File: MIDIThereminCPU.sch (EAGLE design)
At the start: 5 parts, among them Q1 16MHz, U1 ATMEGA328P-AU

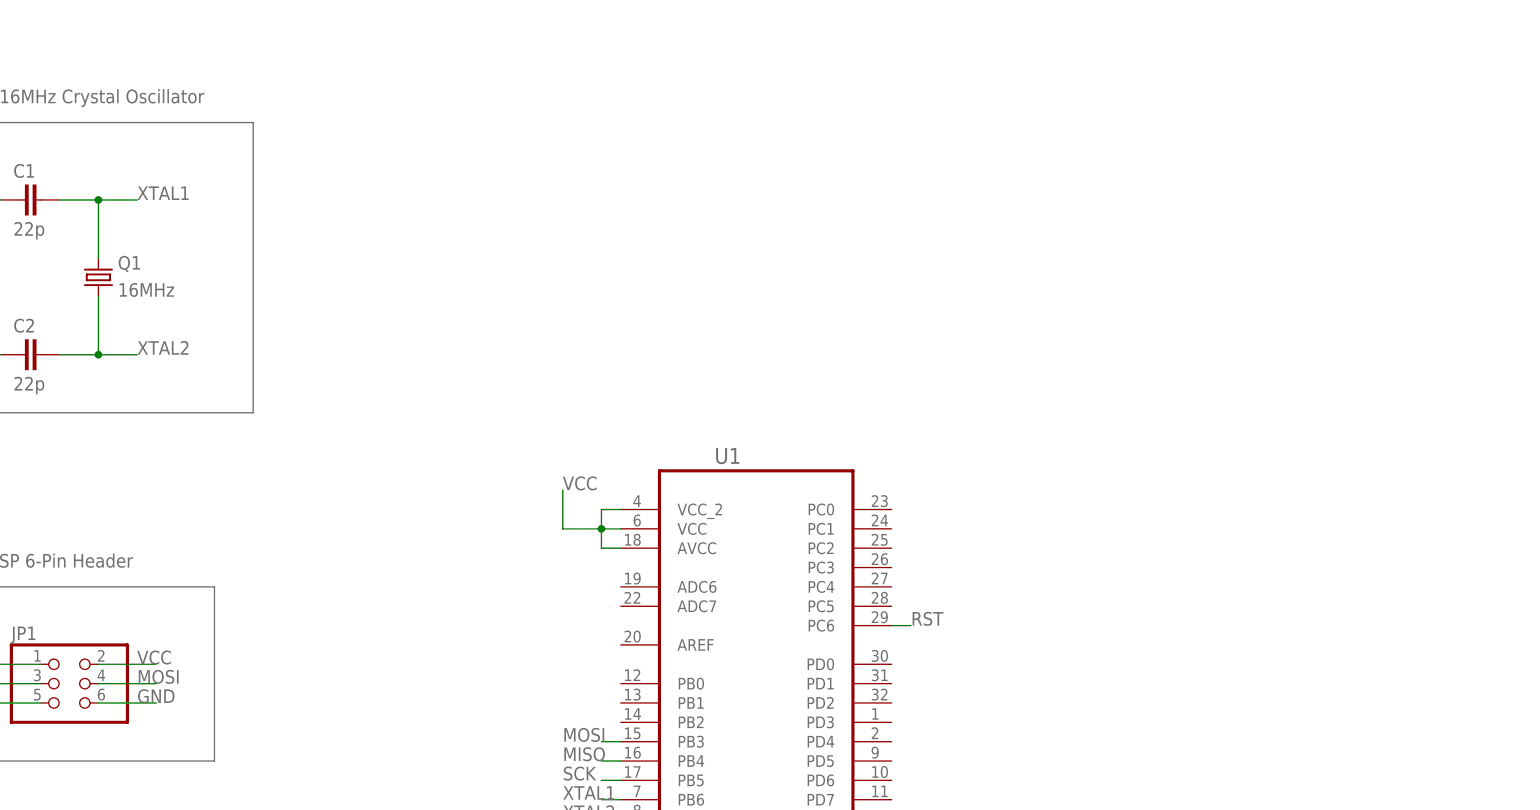
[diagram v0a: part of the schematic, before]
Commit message: Added power input
Added DC barrel jack and 5v and 3.3v regulated sources
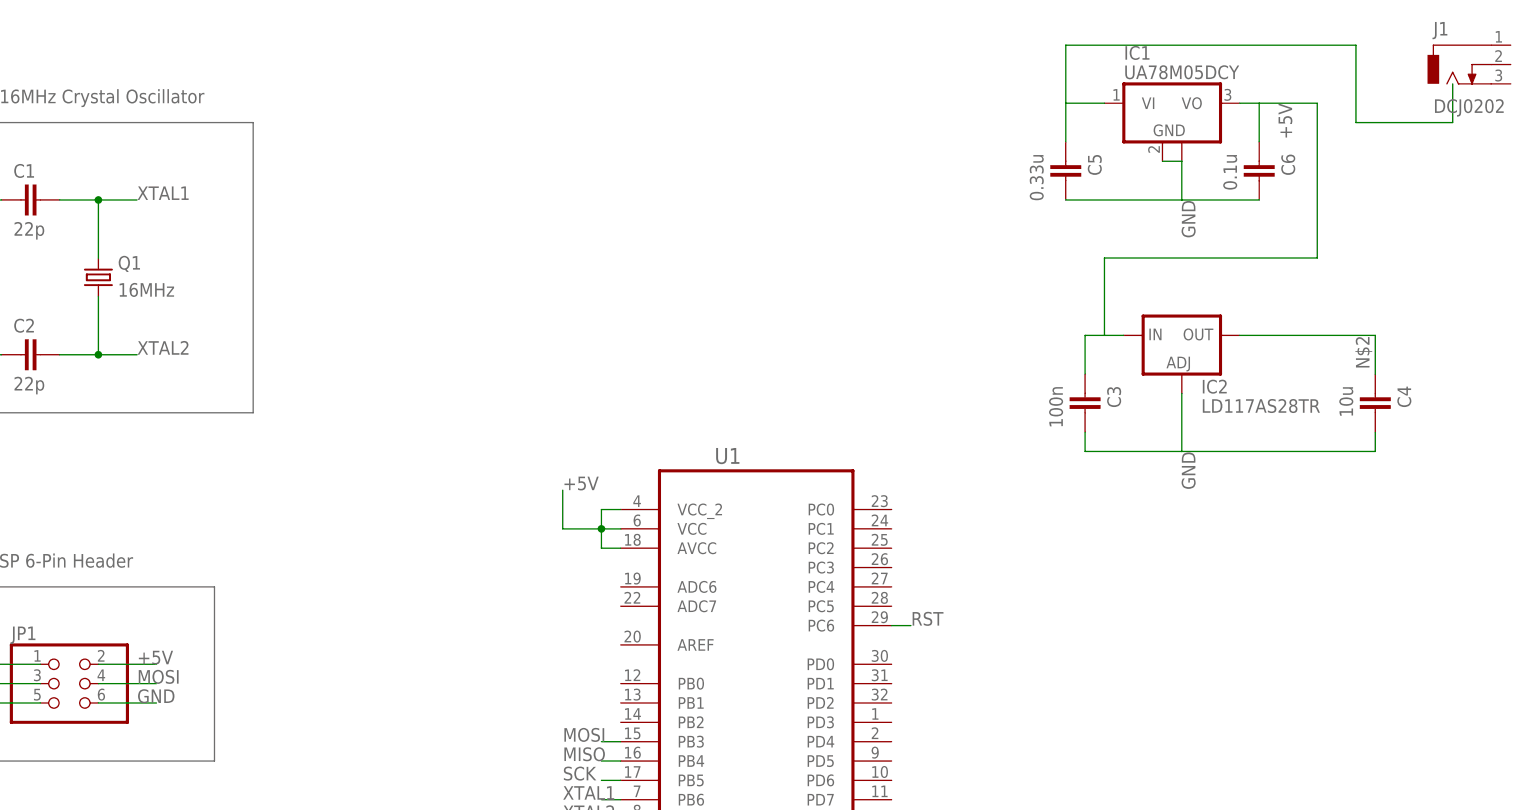
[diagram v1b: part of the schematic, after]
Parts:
- added C3: 100n, capacitor-wima:C2,5-3
- added C4: 10u, capacitor-wima:C2,5-3
- added C5: 0.33u, capacitor-wima:C2,5-3
- added C6: 0.1u, capacitor-wima:C2,5-3
- added IC1: UA78M05DCY, linear:UA78M05DCY
- added IC2: LD117AS28TR, v-reg:LD117AS28TR
- added J1: DCJ0202, con-jack:DCJ0202
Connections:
- removed net VCC: JP1.2, U1.AVCC, U1.VCC, U1.VCC_2
- new net +5V: C3.1, C6.1, IC1.VO, IC2.IN, JP1.2, U1.AVCC, U1.VCC, U1.VCC_2
- new net N$2: C4.1, IC2.OUT
- new net N$5: C5.1, IC1.VI
- net GND: now also C3.2, C4.2, C5.2, C6.2, IC1.GND, IC1.GND@1, IC2.ADJ

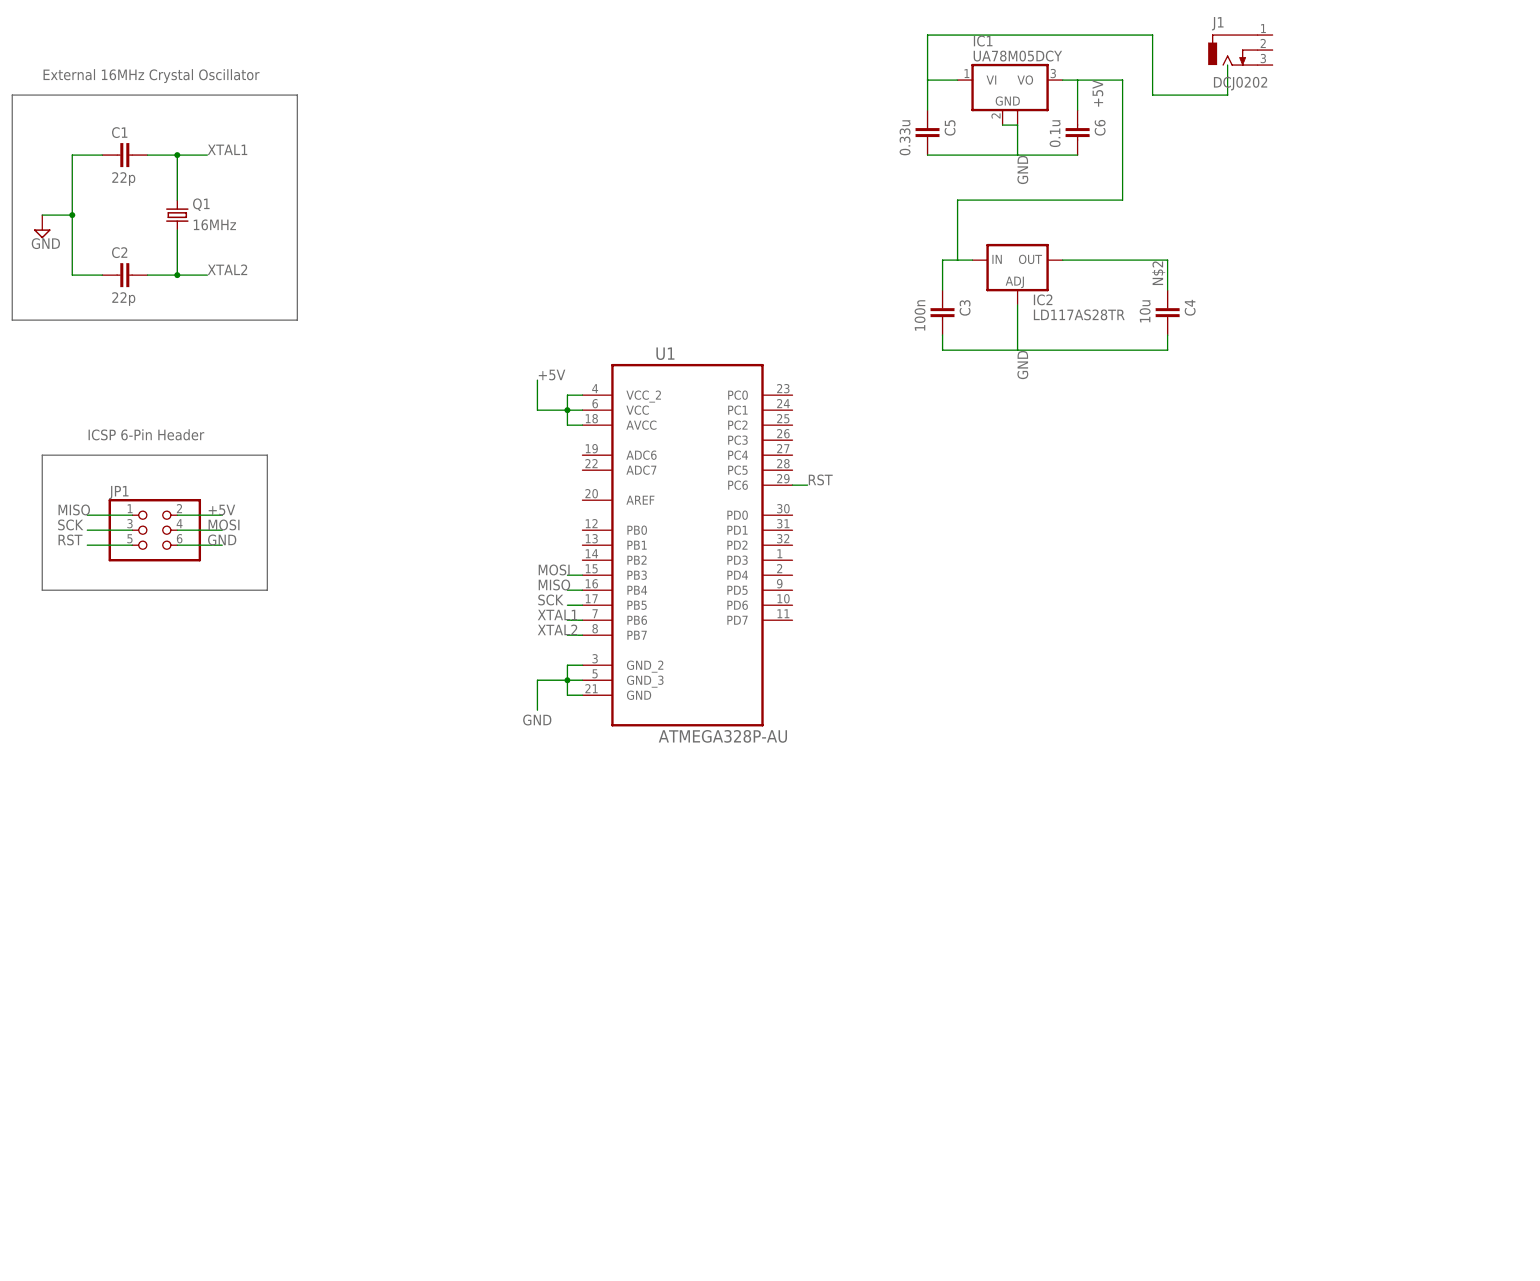
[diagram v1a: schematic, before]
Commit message: Labeled power section and added MIDI I/O
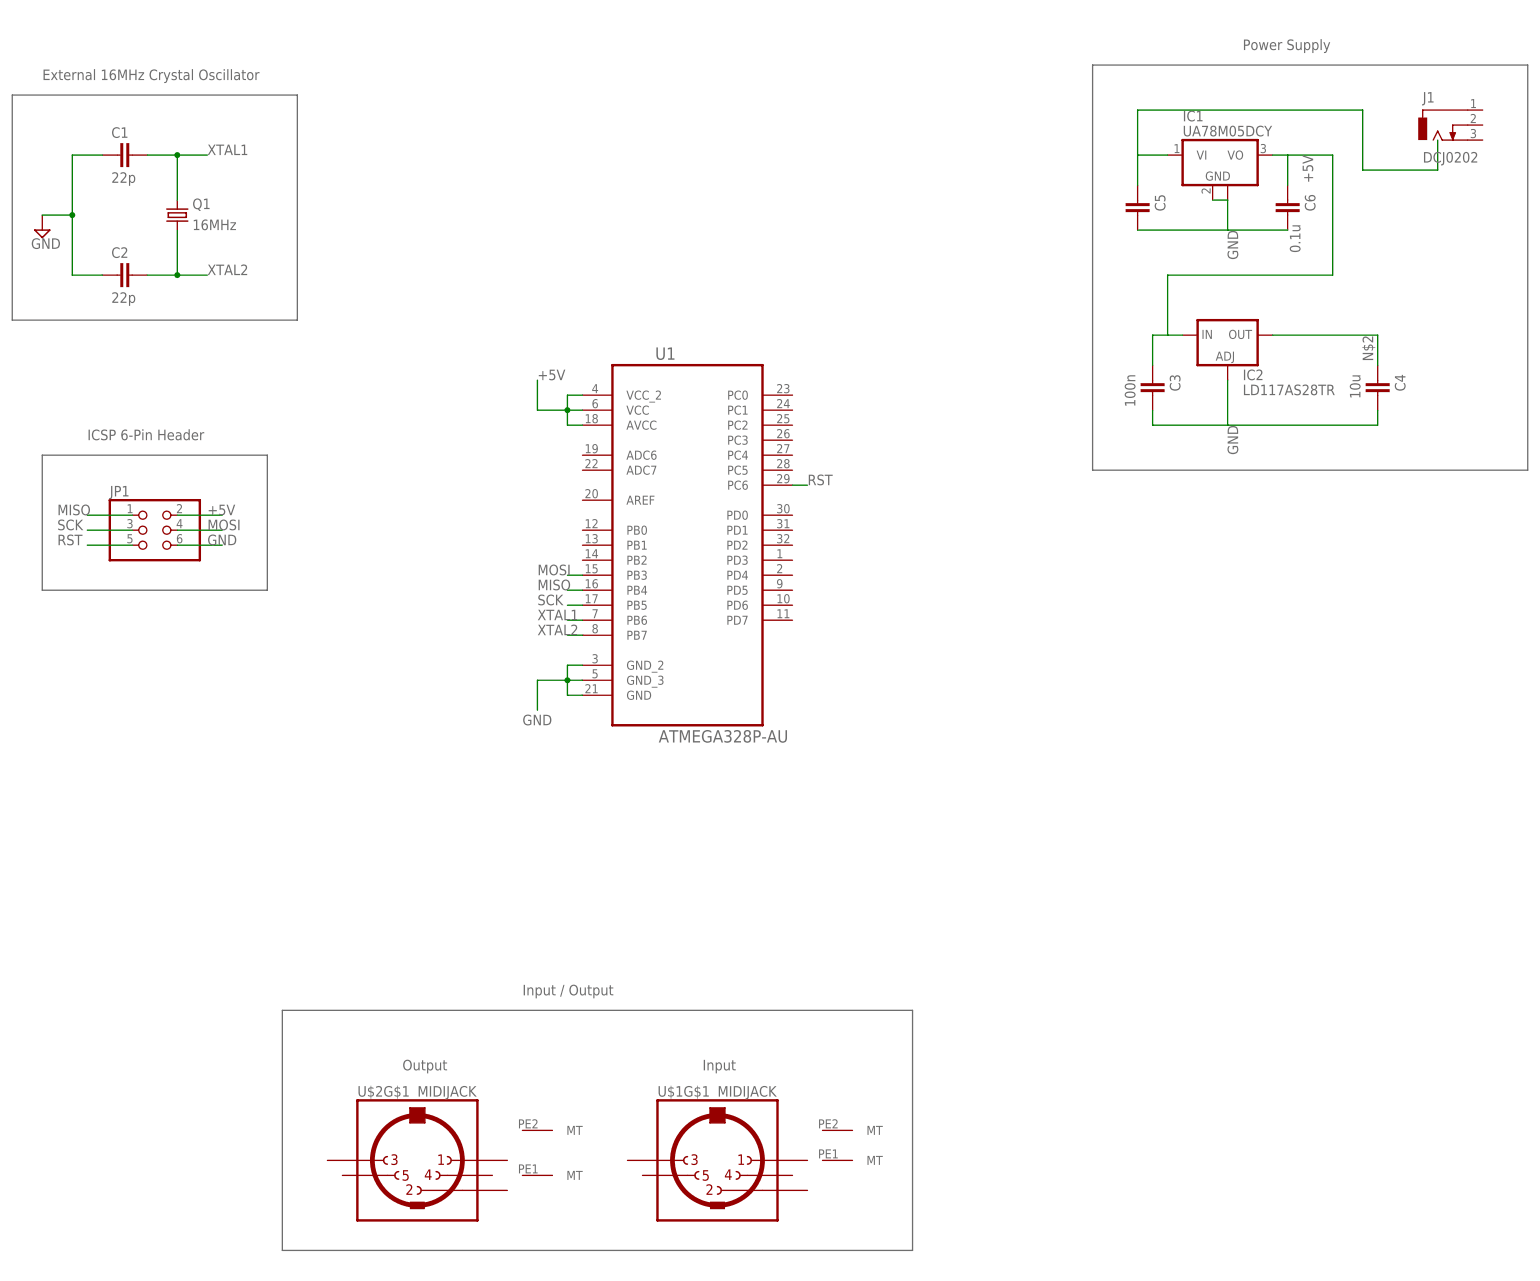
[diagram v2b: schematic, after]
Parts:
- added U$1, U$2: MIDIJACK, adafruit:MIDIJACK
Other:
- note added: "Input"
- note added: "Input / Output"
- note added: "Output"
- note added: "Power Supply"
- moved on the sheet: C3, C4, C5, C6, IC1, IC2, J1

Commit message: Removed 3.3V, connected MIDI
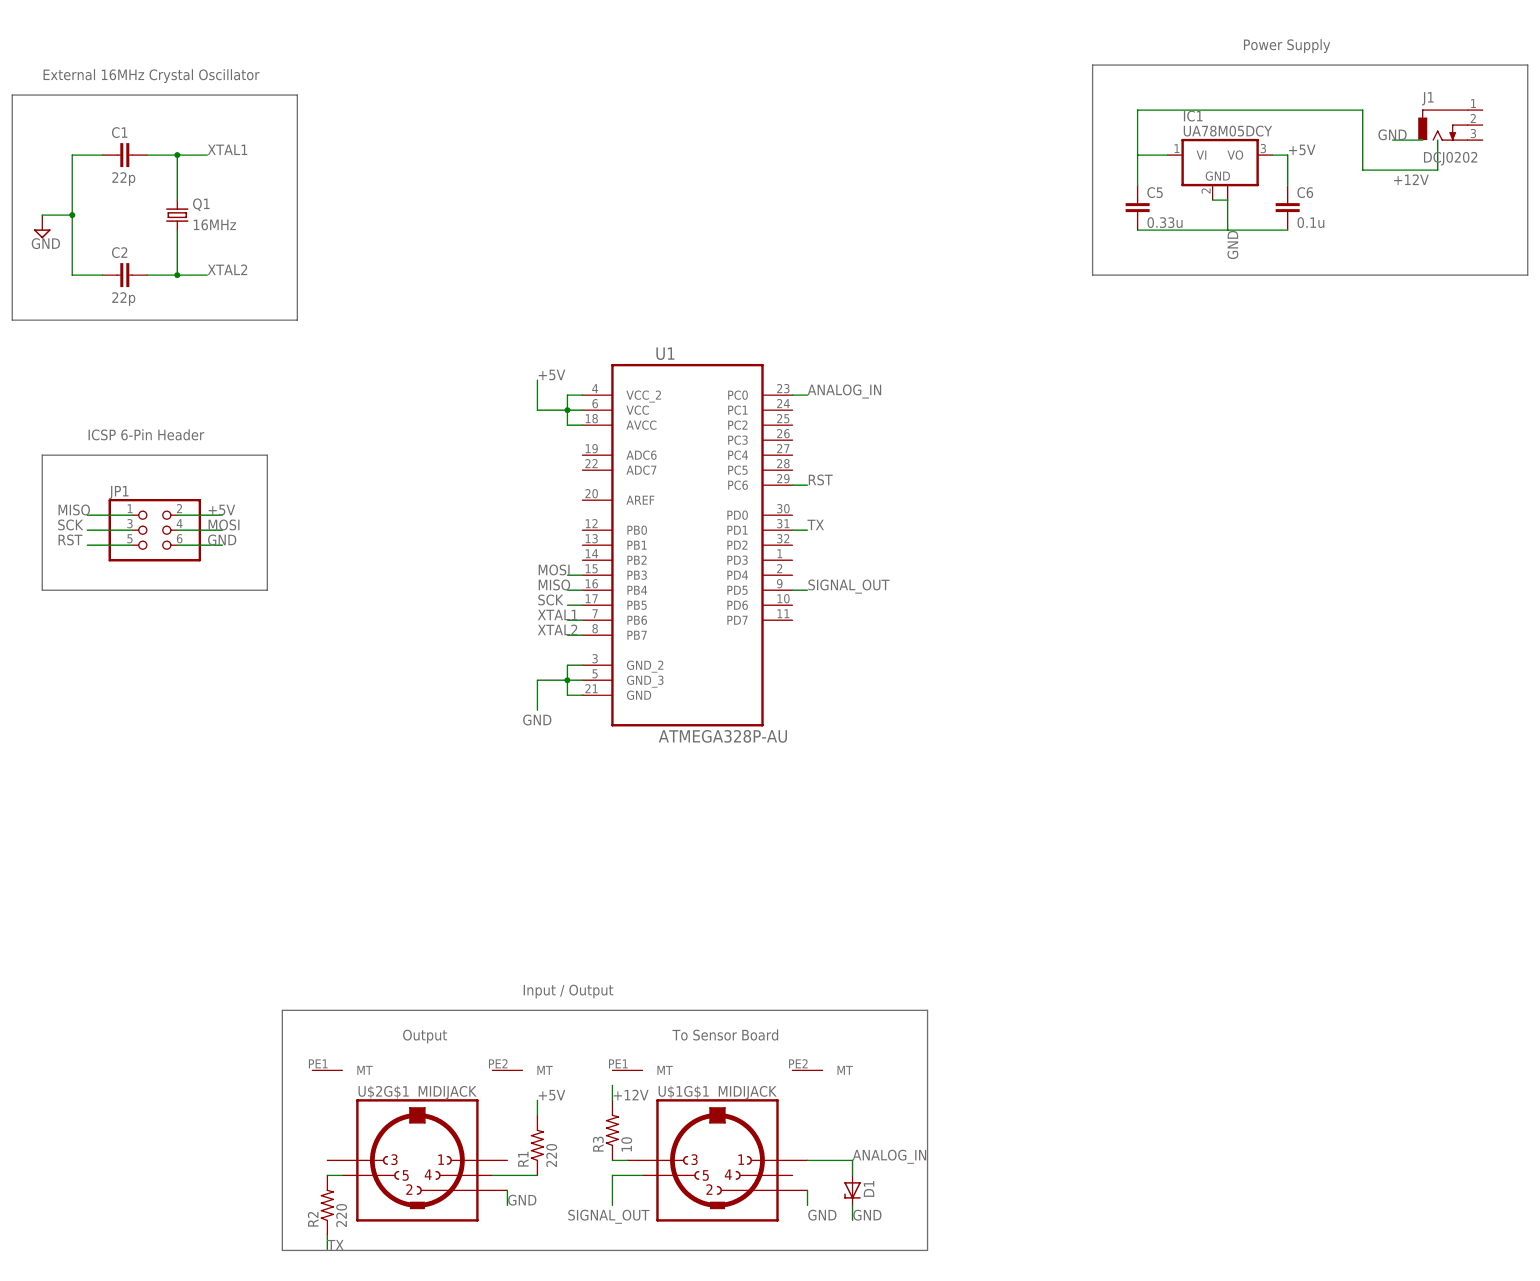
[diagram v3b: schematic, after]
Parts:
- removed C3: 100n, capacitor-wima:C2,5-3
- removed C4: 10u, capacitor-wima:C2,5-3
- removed IC2: LD117AS28TR, v-reg:LD117AS28TR
- added D1: (no value), diode:ZENER-DIODEP1-Z12
- added R1, R2: 220, resistor:R-US_0207/10
- added R3: 10, resistor:R-US_0207/10
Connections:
- removed net N$5: C5.1, IC1.VI
- new net +12V: C5.1, IC1.VI, R3.2
- new net ANALOG_IN: D1.A, U$1G$1.1, U1.PC0
- new net N$1: R1.1, U$2G$1.4
- new net N$3: R3.1, U$1G$1.3
- new net SIGNAL_OUT: U$1G$1.5, U1.PD5
- new net TX: R2.1, U1.PD1
- net +5V: now also R1.2; no longer C3.1, IC2.IN
- net GND: now also D1.C, U$1G$1.2, U$2G$1.2; no longer C3.2, C4.2, IC2.ADJ
- net N$2: now also R2.2, U$2G$1.5; no longer C4.1, IC2.OUT
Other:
- note added: "To Sensor Board"
- note removed: "Input"
